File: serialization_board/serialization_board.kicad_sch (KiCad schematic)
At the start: 24 parts, among them J1 3.3V IN, J2 I2C, J3 INT, J5 I2C stack, J6 3.3V stack, J7 I2C stack, J8 3.3V stack, U1 MCP_X

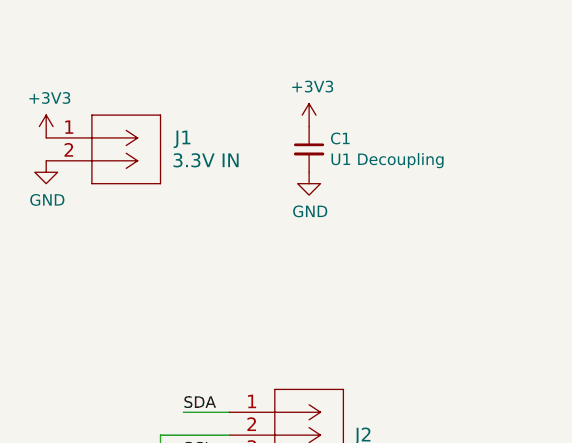
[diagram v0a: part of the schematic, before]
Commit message: Specified decoupling cap value
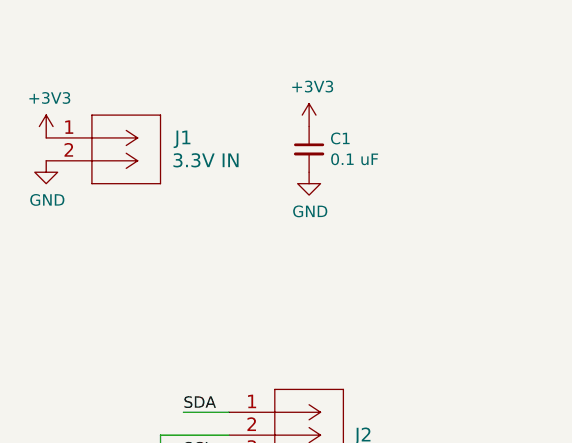
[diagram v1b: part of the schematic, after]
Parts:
- C1: value U1 Decoupling -> 0.1 uF
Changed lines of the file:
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@@
 			)
 		)
-		(property "Value" "U1 Decoupling"
+		(property "Value" "0.1 uF"
 			(at 246.1768 51.943 0)
 			(effects
